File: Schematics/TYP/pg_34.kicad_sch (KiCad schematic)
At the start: 16 parts, among them U3601 F240, U3602 F240, U3603 F240, U3604 F240, U3605 F240, U3606 F240, U3607 F240, U3608 F240, U3609 F240, U3610 F240, U3611 F240, U3612 F240, U3613 F240, U3614 F240, U3615 F240, U3616 F240

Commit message: Megacomp'ification
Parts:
- removed U3604, U3605, U3606, U3607, U3608, U3609, U3610, U3611, U3612, U3613, U3614, U3615, U3616: F240, symbol r1000:F240
- U3601: value F240 -> XBUF64; symbol r1000:F240 -> r1000:XBUF64; Location A40 -> x99; Name FDRV0 -> FDRV
- U3602: value F240 -> XBUF32; symbol r1000:F240 -> r1000:XBUF32; Location A39 -> x99; Name FDRV1 -> FRCVH
- U3603: value F240 -> XBUF32; symbol r1000:F240 -> r1000:XBUF32; Location A36 -> x99; Name FDRV2 -> FRCVL
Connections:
- net A.D0: now also U3601.3 (I0); no longer U3601.11 (I4)
- net A.D1: now also U3601.5 (I1); no longer U3601.13 (I5)
- net A.D10: now also U3601.23 (I10); no longer U3603.15 (I6)
- net A.D11: now also U3601.25 (I11); no longer U3603.17 (I7)
- net A.D12: now also U3601.27 (I12)
- net A.D13: now also U3601.29 (I13)
- net A.D14: now also U3601.31 (I14)
- net A.D15: now also U3601.33 (I15)
- net A.D16: now also U3601.35 (I16)
- net A.D17: now also U3601.37 (I17)
- net A.D18: now also U3601.39 (I18)
- net A.D19: now also U3601.41 (I19)
- net A.D2: now also U3601.7 (I2); no longer U3601.15 (I6)
- net A.D20: now also U3601.43 (I20)
- net A.D21: now also U3601.45 (I21)
- net A.D22: now also U3601.47 (I22)
- net A.D23: now also U3601.49 (I23)
- net A.D24: now also U3601.51 (I24)
- net A.D25: now also U3601.53 (I25)
- net A.D26: now also U3601.55 (I26)
- net A.D27: now also U3601.57 (I27)
- net A.D28: now also U3601.59 (I28)
- net A.D29: now also U3601.61 (I29)
- net A.D3: now also U3601.9 (I3); no longer U3601.17 (I7)
- net A.D30: now also U3601.63 (I30)
- net A.D31: now also U3601.65 (I31)
- net A.D32: now also U3601.67 (I32)
- net A.D33: now also U3601.69 (I33)
- net A.D34: now also U3601.71 (I34)
- net A.D35: now also U3601.73 (I35)
- net A.D36: now also U3601.75 (I36)
- net A.D37: now also U3601.77 (I37)
- net A.D38: now also U3601.79 (I38)
- net A.D39: now also U3601.81 (I39)
- net A.D4: now also U3601.11 (I4); no longer U3602.11 (I4)
- net A.D40: now also U3601.83 (I40)
- net A.D41: now also U3601.85 (I41)
- net A.D42: now also U3601.87 (I42)
- net A.D43: now also U3601.89 (I43)
- net A.D44: now also U3601.91 (I44)
- net A.D45: now also U3601.93 (I45)
- net A.D46: now also U3601.95 (I46)
- net A.D47: now also U3601.97 (I47)
- net A.D48: now also U3601.99 (I48)
- net A.D49: now also U3601.101 (I49)
- net A.D5: now also U3601.13 (I5); no longer U3602.13 (I5)
- net A.D50: now also U3601.103 (I50)
- net A.D51: now also U3601.105 (I51)
- net A.D52: now also U3601.107 (I52)
- net A.D53: now also U3601.109 (I53)
- net A.D54: now also U3601.111 (I54)
- net A.D55: now also U3601.113 (I55)
- net A.D56: now also U3601.115 (I56)
- net A.D57: now also U3601.117 (I57)
- net A.D58: now also U3601.119 (I58)
- net A.D59: now also U3601.121 (I59)
- net A.D6: now also U3601.15 (I6); no longer U3602.15 (I6)
- net A.D60: now also U3601.123 (I60)
- net A.D61: now also U3601.125 (I61)
- net A.D62: now also U3601.127 (I62)
- net A.D63: now also U3601.129 (I63)
- net A.D7: now also U3601.17 (I7); no longer U3602.17 (I7)
- net A.D8: now also U3601.19 (I8); no longer U3603.11 (I4)
- net A.D9: now also U3601.21 (I9); no longer U3603.13 (I5)
- net C.D0: now also U3602.4 (Y0); no longer U3601.18 (Y0)
- net C.D1: now also U3602.6 (Y1); no longer U3601.16 (Y1)
- net C.D10: now also U3602.24 (Y10); no longer U3603.14 (Y2)
- net C.D11: now also U3602.26 (Y11); no longer U3603.12 (Y3)
- net C.D12: now also U3602.28 (Y12)
- net C.D13: now also U3602.30 (Y13)
- net C.D14: now also U3602.32 (Y14)
- net C.D15: now also U3602.34 (Y15)
- net C.D16: now also U3602.36 (Y16)
- net C.D17: now also U3602.38 (Y17)
- net C.D18: now also U3602.40 (Y18)
- net C.D19: now also U3602.42 (Y19)
- net C.D2: now also U3602.8 (Y2); no longer U3601.14 (Y2)
- net C.D20: now also U3602.44 (Y20)
- net C.D21: now also U3602.46 (Y21)
- net C.D22: now also U3602.48 (Y22)
- net C.D23: now also U3602.50 (Y23)
- net C.D24: now also U3602.52 (Y24)
- net C.D25: now also U3602.54 (Y25)
- net C.D26: now also U3602.56 (Y26)
- net C.D27: now also U3602.58 (Y27)
- net C.D28: now also U3602.60 (Y28)
- net C.D29: now also U3602.62 (Y29)
- net C.D3: now also U3602.10 (Y3); no longer U3601.12 (Y3)
- net C.D30: now also U3602.64 (Y30)
- net C.D31: now also U3602.66 (Y31)
- net C.D32: now also U3603.4 (Y0)
- net C.D33: now also U3603.6 (Y1)
- net C.D34: now also U3603.8 (Y2)
- net C.D35: now also U3603.10 (Y3)
- net C.D36: now also U3603.12 (Y4)
- net C.D37: now also U3603.14 (Y5)
- net C.D38: now also U3603.16 (Y6)
- net C.D39: now also U3603.18 (Y7)
- net C.D4: now also U3602.12 (Y4); no longer U3602.18 (Y0)
- net C.D40: now also U3603.20 (Y8)
- net C.D41: now also U3603.22 (Y9)
- net C.D42: now also U3603.24 (Y10)
- net C.D43: now also U3603.26 (Y11)
- net C.D44: now also U3603.28 (Y12)
- net C.D45: now also U3603.30 (Y13)
- net C.D46: now also U3603.32 (Y14)
- net C.D47: now also U3603.34 (Y15)
- net C.D48: now also U3603.36 (Y16)
- net C.D49: now also U3603.38 (Y17)
- net C.D5: now also U3602.14 (Y5); no longer U3602.16 (Y1)
- net C.D50: now also U3603.40 (Y18)
- net C.D51: now also U3603.42 (Y19)
- net C.D52: now also U3603.44 (Y20)
- net C.D53: now also U3603.46 (Y21)
- net C.D54: now also U3603.48 (Y22)
- net C.D55: now also U3603.50 (Y23)
- net C.D56: now also U3603.52 (Y24)
- net C.D57: now also U3603.54 (Y25)
- net C.D58: now also U3603.56 (Y26)
- net C.D59: now also U3603.58 (Y27)
- net C.D6: now also U3602.16 (Y6); no longer U3602.14 (Y2)
- net C.D60: now also U3603.60 (Y28)
- net C.D61: now also U3603.62 (Y29)
- net C.D62: now also U3603.64 (Y30)
- net C.D63: now also U3603.66 (Y31)
- net C.D7: now also U3602.18 (Y7); no longer U3602.12 (Y3)
- net C.D8: now also U3602.20 (Y8); no longer U3603.18 (Y0)
- net C.D9: now also U3602.22 (Y9); no longer U3603.16 (Y1)
- net C_FIU.OE~0: now also U3602.2 (OE); no longer U3601.1 (OE0), U3602.1 (OE0), U3603.1 (OE0)
- net C_FIU.OE~1: now also U3603.2 (OE)
- net FIU.OE~: now also U3601.2 (OE); no longer U3601.19 (OE1), U3602.19 (OE1), U3603.19 (OE1)
- net T.FIU.D0: now also U3601.4 (Y0), U3602.3 (I0); no longer U3601.2 (I0), U3601.9 (Y4)
- net T.FIU.D1: now also U3601.6 (Y1), U3602.5 (I1); no longer U3601.4 (I1), U3601.7 (Y5)
- net T.FIU.D10: now also U3601.24 (Y10), U3602.23 (I10); no longer U3603.5 (Y6), U3603.6 (I2)
- net T.FIU.D11: now also U3601.26 (Y11), U3602.25 (I11); no longer U3603.3 (Y7), U3603.8 (I3)
- net T.FIU.D12: now also U3601.28 (Y12), U3602.27 (I12)
- net T.FIU.D13: now also U3601.30 (Y13), U3602.29 (I13)
- net T.FIU.D14: now also U3601.32 (Y14), U3602.31 (I14)
- net T.FIU.D15: now also U3601.34 (Y15), U3602.33 (I15)
- net T.FIU.D16: now also U3601.36 (Y16), U3602.35 (I16)
- net T.FIU.D17: now also U3601.38 (Y17), U3602.37 (I17)
- net T.FIU.D18: now also U3601.40 (Y18), U3602.39 (I18)
- net T.FIU.D19: now also U3601.42 (Y19), U3602.41 (I19)
- net T.FIU.D2: now also U3601.8 (Y2), U3602.7 (I2); no longer U3601.5 (Y6), U3601.6 (I2)
- net T.FIU.D20: now also U3601.44 (Y20), U3602.43 (I20)
- net T.FIU.D21: now also U3601.46 (Y21), U3602.45 (I21)
- net T.FIU.D22: now also U3601.48 (Y22), U3602.47 (I22)
- net T.FIU.D23: now also U3601.50 (Y23), U3602.49 (I23)
- net T.FIU.D24: now also U3601.52 (Y24), U3602.51 (I24)
- net T.FIU.D25: now also U3601.54 (Y25), U3602.53 (I25)
- net T.FIU.D26: now also U3601.56 (Y26), U3602.55 (I26)
- net T.FIU.D27: now also U3601.58 (Y27), U3602.57 (I27)
- net T.FIU.D28: now also U3601.60 (Y28), U3602.59 (I28)
- net T.FIU.D29: now also U3601.62 (Y29), U3602.61 (I29)
- net T.FIU.D3: now also U3601.10 (Y3), U3602.9 (I3); no longer U3601.3 (Y7), U3601.8 (I3)
- net T.FIU.D30: now also U3601.64 (Y30), U3602.63 (I30)
- net T.FIU.D31: now also U3601.66 (Y31), U3602.65 (I31)
- net T.FIU.D32: now also U3601.68 (Y32), U3603.3 (I0)
- net T.FIU.D33: now also U3601.70 (Y33), U3603.5 (I1)
- net T.FIU.D34: now also U3601.72 (Y34), U3603.7 (I2)
- net T.FIU.D35: now also U3601.74 (Y35), U3603.9 (I3)
- net T.FIU.D36: now also U3601.76 (Y36), U3603.11 (I4)
- net T.FIU.D37: now also U3601.78 (Y37), U3603.13 (I5)
- net T.FIU.D38: now also U3601.80 (Y38), U3603.15 (I6)
- net T.FIU.D39: now also U3601.82 (Y39), U3603.17 (I7)
- net T.FIU.D4: now also U3601.12 (Y4), U3602.11 (I4); no longer U3602.2 (I0), U3602.9 (Y4)
- net T.FIU.D40: now also U3601.84 (Y40), U3603.19 (I8)
- net T.FIU.D41: now also U3601.86 (Y41), U3603.21 (I9)
- net T.FIU.D42: now also U3601.88 (Y42), U3603.23 (I10)
- net T.FIU.D43: now also U3601.90 (Y43), U3603.25 (I11)
- net T.FIU.D44: now also U3601.92 (Y44), U3603.27 (I12)
- net T.FIU.D45: now also U3601.94 (Y45), U3603.29 (I13)
- net T.FIU.D46: now also U3601.96 (Y46), U3603.31 (I14)
- net T.FIU.D47: now also U3601.98 (Y47), U3603.33 (I15)
- net T.FIU.D48: now also U3601.100 (Y48), U3603.35 (I16)
- net T.FIU.D49: now also U3601.102 (Y49), U3603.37 (I17)
- net T.FIU.D5: now also U3601.14 (Y5), U3602.13 (I5); no longer U3602.4 (I1), U3602.7 (Y5)
- net T.FIU.D50: now also U3601.104 (Y50), U3603.39 (I18)
- net T.FIU.D51: now also U3601.106 (Y51), U3603.41 (I19)
- net T.FIU.D52: now also U3601.108 (Y52), U3603.43 (I20)
- net T.FIU.D53: now also U3601.110 (Y53), U3603.45 (I21)
- net T.FIU.D54: now also U3601.112 (Y54), U3603.47 (I22)
- net T.FIU.D55: now also U3601.114 (Y55), U3603.49 (I23)
- net T.FIU.D56: now also U3601.116 (Y56), U3603.51 (I24)
- net T.FIU.D57: now also U3601.118 (Y57), U3603.53 (I25)
- net T.FIU.D58: now also U3601.120 (Y58), U3603.55 (I26)
- net T.FIU.D59: now also U3601.122 (Y59), U3603.57 (I27)
- net T.FIU.D6: now also U3601.16 (Y6), U3602.15 (I6); no longer U3602.5 (Y6), U3602.6 (I2)
- net T.FIU.D60: now also U3601.124 (Y60), U3603.59 (I28)
- net T.FIU.D61: now also U3601.126 (Y61), U3603.61 (I29)
- net T.FIU.D62: now also U3601.128 (Y62), U3603.63 (I30)
- net T.FIU.D63: now also U3601.130 (Y63), U3603.65 (I31)
- net T.FIU.D7: now also U3601.18 (Y7), U3602.17 (I7); no longer U3602.3 (Y7), U3602.8 (I3)
- net T.FIU.D8: now also U3601.20 (Y8), U3602.19 (I8); no longer U3603.2 (I0), U3603.9 (Y4)
- net T.FIU.D9: now also U3601.22 (Y9), U3602.21 (I9); no longer U3603.4 (I1), U3603.7 (Y5)
- new net PD: U3601.1 (INV), U3602.1 (INV), U3603.1 (INV)

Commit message: KiCad 6
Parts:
- U3601: value XBUF64 -> (none)
- U3602, U3603: value XBUF32 -> (none)

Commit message: Recover from KiCad-6 munging
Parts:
- U3601: value (none) -> XBUF64
- U3602, U3603: value (none) -> XBUF32

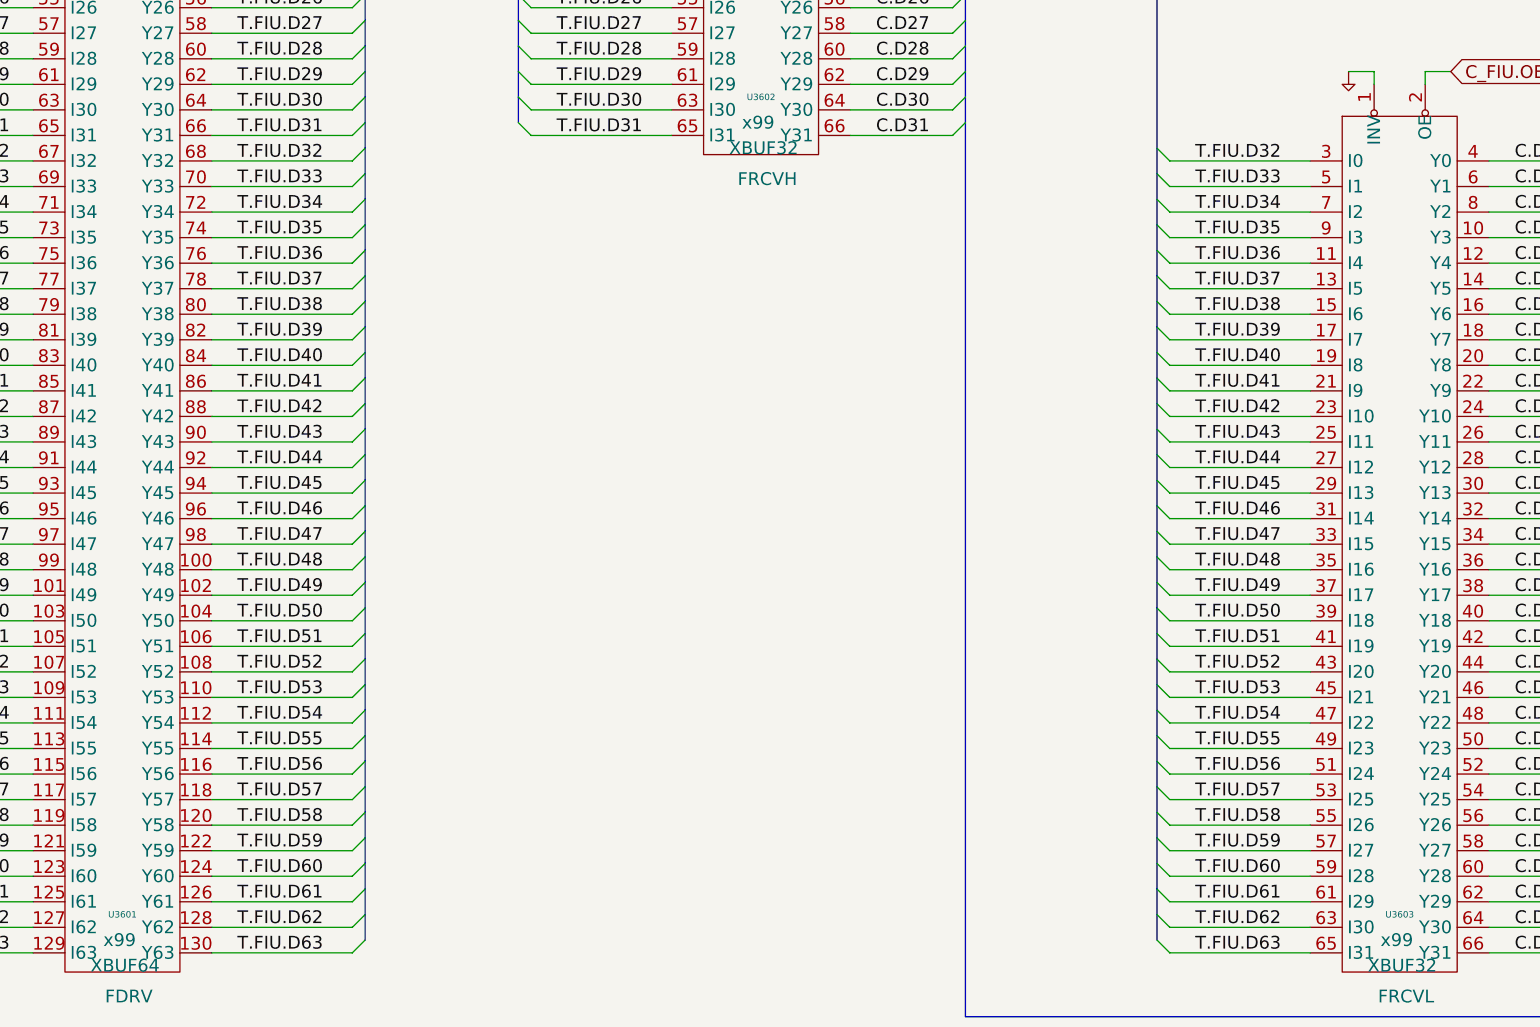
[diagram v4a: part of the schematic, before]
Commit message: Fix H2 signal to global on pg40
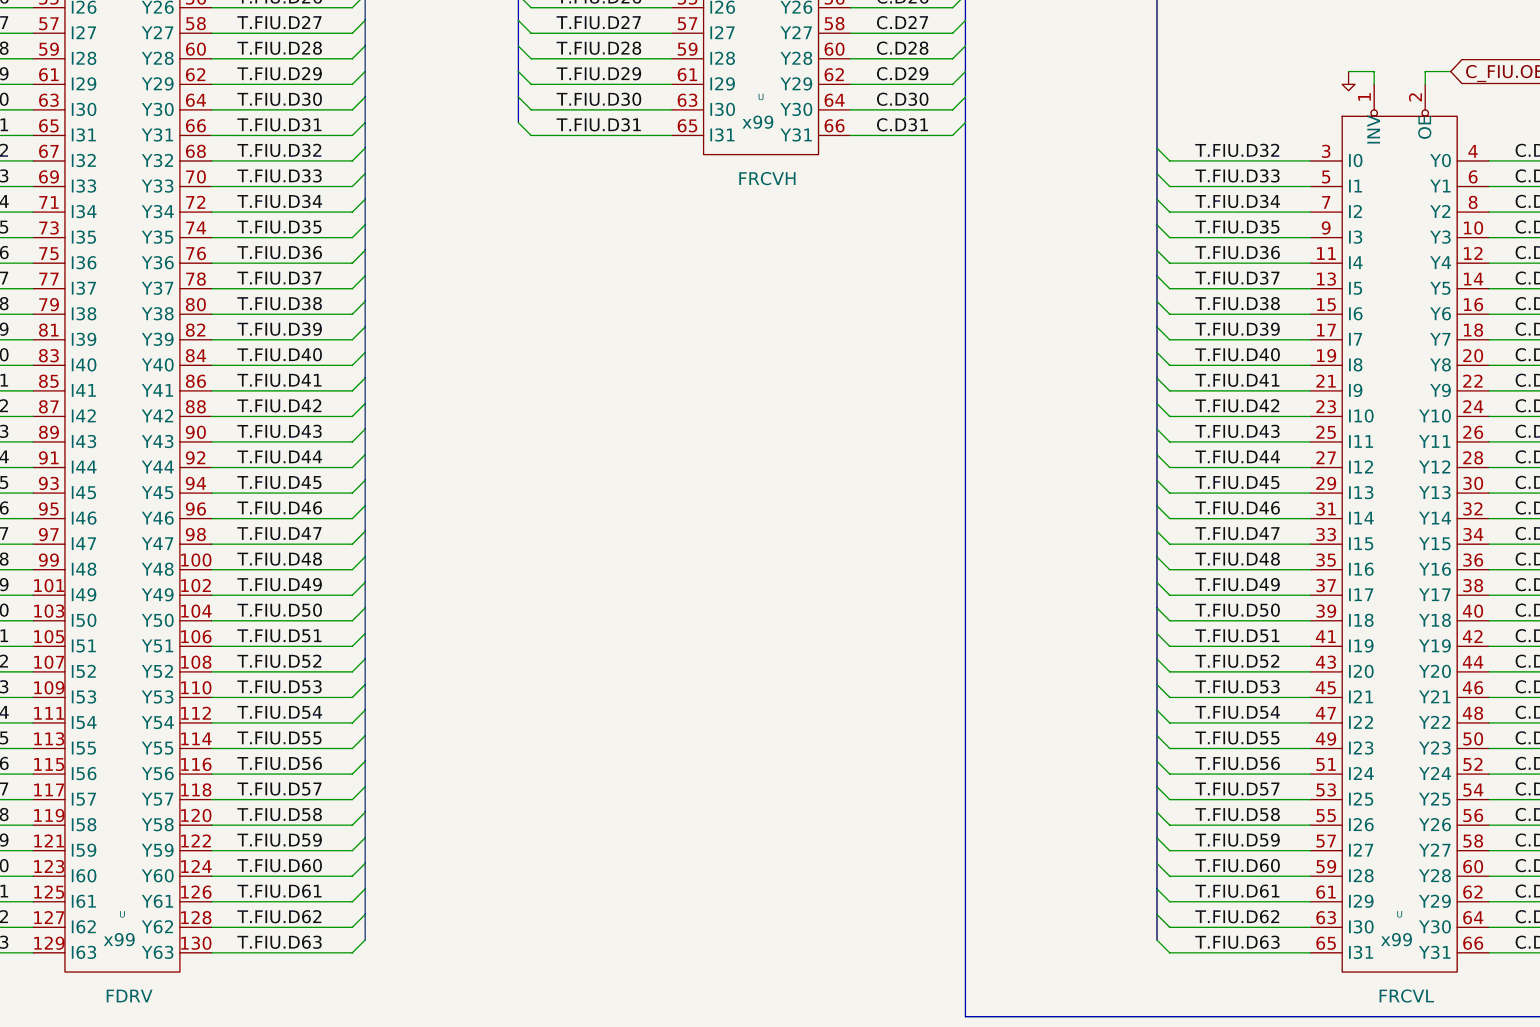
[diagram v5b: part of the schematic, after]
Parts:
- removed U3601: XBUF64, symbol r1000:XBUF64
- removed U3602, U3603: XBUF32, symbol r1000:XBUF32
- added U: (no value), symbol r1000:XBUF64
- added U (x2): (no value), symbol r1000:XBUF32
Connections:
- net A.D0: now also U.3 (I0)
- net A.D1: now also U.5 (I1)
- net A.D10: now also U.23 (I10)
- net A.D11: now also U.25 (I11)
- net A.D12: now also U.27 (I12)
- net A.D13: now also U.29 (I13)
- net A.D14: now also U.31 (I14)
- net A.D15: now also U.33 (I15)
- net A.D16: now also U.35 (I16)
- net A.D17: now also U.37 (I17)
- net A.D18: now also U.39 (I18)
- net A.D19: now also U.41 (I19)
- net A.D2: now also U.7 (I2)
- net A.D20: now also U.43 (I20)
- net A.D21: now also U.45 (I21)
- net A.D22: now also U.47 (I22)
- net A.D23: now also U.49 (I23)
- net A.D24: now also U.51 (I24)
- net A.D25: now also U.53 (I25)
- net A.D26: now also U.55 (I26)
- net A.D27: now also U.57 (I27)
- net A.D28: now also U.59 (I28)
- net A.D29: now also U.61 (I29)
- net A.D3: now also U.9 (I3)
- net A.D30: now also U.63 (I30)
- net A.D31: now also U.65 (I31)
- net A.D32: now also U.67 (I32)
- net A.D33: now also U.69 (I33)
- net A.D34: now also U.71 (I34)
- net A.D35: now also U.73 (I35)
- net A.D36: now also U.75 (I36)
- net A.D37: now also U.77 (I37)
- net A.D38: now also U.79 (I38)
- net A.D39: now also U.81 (I39)
- net A.D4: now also U.11 (I4)
- net A.D40: now also U.83 (I40)
- net A.D41: now also U.85 (I41)
- net A.D42: now also U.87 (I42)
- net A.D43: now also U.89 (I43)
- net A.D44: now also U.91 (I44)
- net A.D45: now also U.93 (I45)
- net A.D46: now also U.95 (I46)
- net A.D47: now also U.97 (I47)
- net A.D48: now also U.99 (I48)
- net A.D49: now also U.101 (I49)
- net A.D5: now also U.13 (I5)
- net A.D50: now also U.103 (I50)
- net A.D51: now also U.105 (I51)
- net A.D52: now also U.107 (I52)
- net A.D53: now also U.109 (I53)
- net A.D54: now also U.111 (I54)
- net A.D55: now also U.113 (I55)
- net A.D56: now also U.115 (I56)
- net A.D57: now also U.117 (I57)
- net A.D58: now also U.119 (I58)
- net A.D59: now also U.121 (I59)
- net A.D6: now also U.15 (I6)
- net A.D60: now also U.123 (I60)
- net A.D61: now also U.125 (I61)
- net A.D62: now also U.127 (I62)
- net A.D63: now also U.129 (I63)
- net A.D7: now also U.17 (I7)
- net A.D8: now also U.19 (I8)
- net A.D9: now also U.21 (I9)
- net C.D0: now also U.4 (Y0)
- net C.D1: now also U.6 (Y1)
- net C.D10: now also U.24 (Y10)
- net C.D11: now also U.26 (Y11)
- net C.D12: now also U.28 (Y12)
- net C.D13: now also U.30 (Y13)
- net C.D14: now also U.32 (Y14)
- net C.D15: now also U.34 (Y15)
- net C.D16: now also U.36 (Y16)
- net C.D17: now also U.38 (Y17)
- net C.D18: now also U.40 (Y18)
- net C.D19: now also U.42 (Y19)
- net C.D2: now also U.8 (Y2)
- net C.D20: now also U.44 (Y20)
- net C.D21: now also U.46 (Y21)
- net C.D22: now also U.48 (Y22)
- net C.D23: now also U.50 (Y23)
- net C.D24: now also U.52 (Y24)
- net C.D25: now also U.54 (Y25)
- net C.D26: now also U.56 (Y26)
- net C.D27: now also U.58 (Y27)
- net C.D28: now also U.60 (Y28)
- net C.D29: now also U.62 (Y29)
- net C.D3: now also U.10 (Y3)
- net C.D30: now also U.64 (Y30)
- net C.D31: now also U.66 (Y31)
- net C.D32: now also U.4 (Y0)
- net C.D33: now also U.6 (Y1)
- net C.D34: now also U.8 (Y2)
- net C.D35: now also U.10 (Y3)
- net C.D36: now also U.12 (Y4)
- net C.D37: now also U.14 (Y5)
- net C.D38: now also U.16 (Y6)
- net C.D39: now also U.18 (Y7)
- net C.D4: now also U.12 (Y4)
- net C.D40: now also U.20 (Y8)
- net C.D41: now also U.22 (Y9)
- net C.D42: now also U.24 (Y10)
- net C.D43: now also U.26 (Y11)
- net C.D44: now also U.28 (Y12)
- net C.D45: now also U.30 (Y13)
- net C.D46: now also U.32 (Y14)
- net C.D47: now also U.34 (Y15)
- net C.D48: now also U.36 (Y16)
- net C.D49: now also U.38 (Y17)
- net C.D5: now also U.14 (Y5)
- net C.D50: now also U.40 (Y18)
- net C.D51: now also U.42 (Y19)
- net C.D52: now also U.44 (Y20)
- net C.D53: now also U.46 (Y21)
- net C.D54: now also U.48 (Y22)
- net C.D55: now also U.50 (Y23)
- net C.D56: now also U.52 (Y24)
- net C.D57: now also U.54 (Y25)
- net C.D58: now also U.56 (Y26)
- net C.D59: now also U.58 (Y27)
- net C.D6: now also U.16 (Y6)
- net C.D60: now also U.60 (Y28)
- net C.D61: now also U.62 (Y29)
- net C.D62: now also U.64 (Y30)
- net C.D63: now also U.66 (Y31)
- net C.D7: now also U.18 (Y7)
- net C.D8: now also U.20 (Y8)
- net C.D9: now also U.22 (Y9)
- net C_FIU.OE~0: now also U.2 (OE)
- net C_FIU.OE~1: now also U.2 (OE)
- net FIU.OE~: now also U.2 (OE)
- net PD: now also U.1 (INV), U.1 (INV), U.1 (INV)
- net T.FIU.D0: now also U.3 (I0), U.4 (Y0)
- net T.FIU.D1: now also U.5 (I1), U.6 (Y1)
- net T.FIU.D10: now also U.23 (I10), U.24 (Y10)
- net T.FIU.D11: now also U.25 (I11), U.26 (Y11)
- net T.FIU.D12: now also U.27 (I12), U.28 (Y12)
- net T.FIU.D13: now also U.29 (I13), U.30 (Y13)
- net T.FIU.D14: now also U.31 (I14), U.32 (Y14)
- net T.FIU.D15: now also U.33 (I15), U.34 (Y15)
- net T.FIU.D16: now also U.35 (I16), U.36 (Y16)
- net T.FIU.D17: now also U.37 (I17), U.38 (Y17)
- net T.FIU.D18: now also U.39 (I18), U.40 (Y18)
- net T.FIU.D19: now also U.41 (I19), U.42 (Y19)
- net T.FIU.D2: now also U.7 (I2), U.8 (Y2)
- net T.FIU.D20: now also U.43 (I20), U.44 (Y20)
- net T.FIU.D21: now also U.45 (I21), U.46 (Y21)
- net T.FIU.D22: now also U.47 (I22), U.48 (Y22)
- net T.FIU.D23: now also U.49 (I23), U.50 (Y23)
- net T.FIU.D24: now also U.51 (I24), U.52 (Y24)
- net T.FIU.D25: now also U.53 (I25), U.54 (Y25)
- net T.FIU.D26: now also U.55 (I26), U.56 (Y26)
- net T.FIU.D27: now also U.57 (I27), U.58 (Y27)
- net T.FIU.D28: now also U.59 (I28), U.60 (Y28)
- net T.FIU.D29: now also U.61 (I29), U.62 (Y29)
- net T.FIU.D3: now also U.10 (Y3), U.9 (I3)
- net T.FIU.D30: now also U.63 (I30), U.64 (Y30)
- net T.FIU.D31: now also U.65 (I31), U.66 (Y31)
- net T.FIU.D32: now also U.3 (I0), U.68 (Y32)
- net T.FIU.D33: now also U.5 (I1), U.70 (Y33)
- net T.FIU.D34: now also U.7 (I2), U.72 (Y34)
- net T.FIU.D35: now also U.74 (Y35), U.9 (I3)
- net T.FIU.D36: now also U.11 (I4), U.76 (Y36)
- net T.FIU.D37: now also U.13 (I5), U.78 (Y37)
- net T.FIU.D38: now also U.15 (I6), U.80 (Y38)
- net T.FIU.D39: now also U.17 (I7), U.82 (Y39)
- net T.FIU.D4: now also U.11 (I4), U.12 (Y4)
- net T.FIU.D40: now also U.19 (I8), U.84 (Y40)
- net T.FIU.D41: now also U.21 (I9), U.86 (Y41)
- net T.FIU.D42: now also U.23 (I10), U.88 (Y42)
- net T.FIU.D43: now also U.25 (I11), U.90 (Y43)
- net T.FIU.D44: now also U.27 (I12), U.92 (Y44)
- net T.FIU.D45: now also U.29 (I13), U.94 (Y45)
- net T.FIU.D46: now also U.31 (I14), U.96 (Y46)
- net T.FIU.D47: now also U.33 (I15), U.98 (Y47)
- net T.FIU.D48: now also U.100 (Y48), U.35 (I16)
- net T.FIU.D49: now also U.102 (Y49), U.37 (I17)
- net T.FIU.D5: now also U.13 (I5), U.14 (Y5)
- net T.FIU.D50: now also U.104 (Y50), U.39 (I18)
- net T.FIU.D51: now also U.106 (Y51), U.41 (I19)
- net T.FIU.D52: now also U.108 (Y52), U.43 (I20)
- net T.FIU.D53: now also U.110 (Y53), U.45 (I21)
- net T.FIU.D54: now also U.112 (Y54), U.47 (I22)
- net T.FIU.D55: now also U.114 (Y55), U.49 (I23)
- net T.FIU.D56: now also U.116 (Y56), U.51 (I24)
- net T.FIU.D57: now also U.118 (Y57), U.53 (I25)
- net T.FIU.D58: now also U.120 (Y58), U.55 (I26)
- net T.FIU.D59: now also U.122 (Y59), U.57 (I27)
- net T.FIU.D6: now also U.15 (I6), U.16 (Y6)
- net T.FIU.D60: now also U.124 (Y60), U.59 (I28)
- net T.FIU.D61: now also U.126 (Y61), U.61 (I29)
- net T.FIU.D62: now also U.128 (Y62), U.63 (I30)
- net T.FIU.D63: now also U.130 (Y63), U.65 (I31)
- net T.FIU.D7: now also U.17 (I7), U.18 (Y7)
- net T.FIU.D8: now also U.19 (I8), U.20 (Y8)
- net T.FIU.D9: now also U.21 (I9), U.22 (Y9)
